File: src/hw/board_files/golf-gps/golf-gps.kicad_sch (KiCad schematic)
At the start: 0 parts

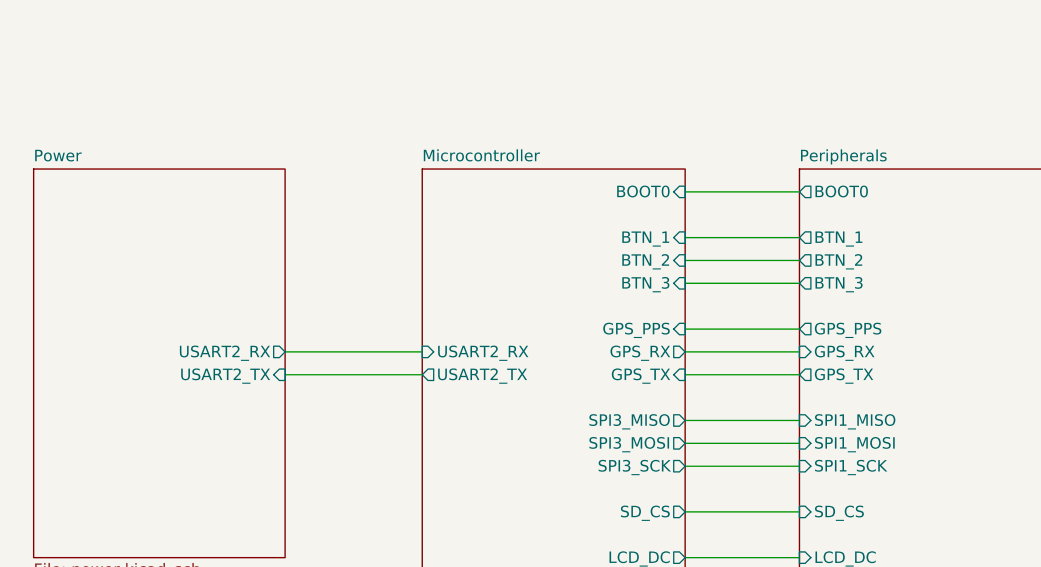
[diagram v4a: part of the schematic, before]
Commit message: Removed USB to UART bridge, added VDDA decoupling, adjusted MCU pinout and updated spreadsheet
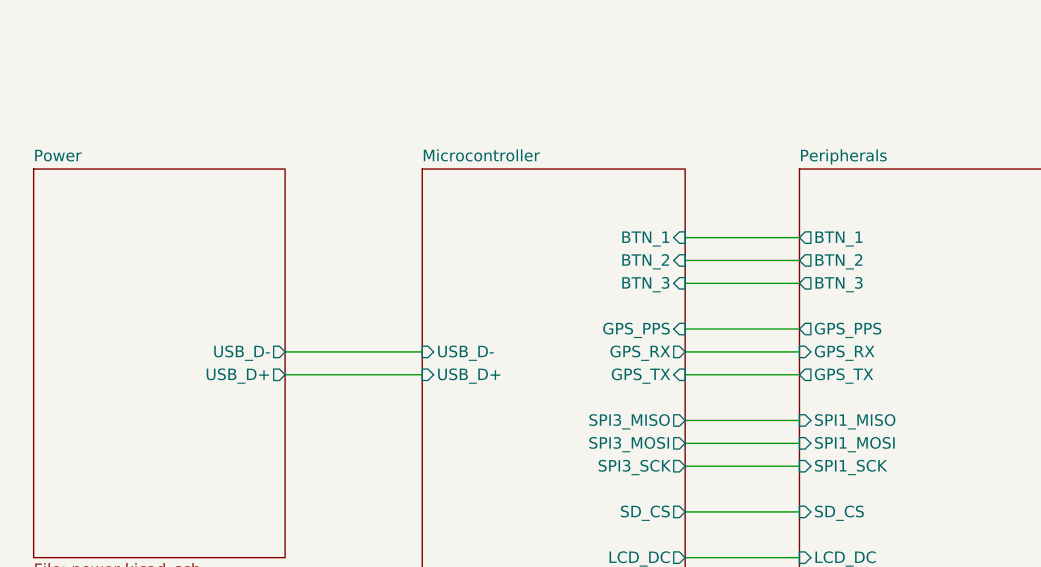
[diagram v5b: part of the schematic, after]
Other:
- sheet Microcontroller ports: added USB_D+, USB_D-; removed BOOT0, USART2_RX, USART2_TX
- sheet Peripherals ports: added none; removed BOOT0
- sheet Power ports: added USB_D+, USB_D-; removed USART2_RX, USART2_TX
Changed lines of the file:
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@@
+	(wire
+		(pts
+			(xy 74.93 80.01) (xy 90.17 80.01)
+		)
+		(stroke
+			(width 0)
+			(type default)
+		)
+	)
 	(wire
 		(pts
@@
 	(wire
 		(pts
-			(xy 74.93 80.01) (xy 90.17 80.01)
-		)
-		(stroke
-			(width 0)
-			(type default)
-		)
-	)
-	(wire
-		(pts
-			(xy 119.38 59.69) (xy 132.08 59.69)
-		)
-		(stroke
-			(width 0)
-			(type default)
-		)
-	)
-	(wire
-		(pts
 			(xy 119.38 85.09) (xy 132.08 85.09)
 		)
@@
 	(wire
 		(pts
+			(xy 74.93 77.47) (xy 90.17 77.47)
+		)
+		(stroke
+			(width 0)
+			(type default)
+		)
+	)
+	(wire
+		(pts
 			(xy 119.38 64.77) (xy 132.08 64.77)
 		)
@@
 		(pts
 			(xy 119.38 95.25) (xy 132.08 95.25)
-		)
-		(stroke
-			(width 0)
-			(type default)
-		)
-	)
-	(wire
-		(pts
-			(xy 74.93 77.47) (xy 90.17 77.47)
 		)
 		(stroke
@@
 			)
 		)
-		(pin "BOOT0" input
-			(at 119.38 59.69 0)
-			(effects
-				(font
-					(size 1.27 1.27)
-				)
-				(justify right)
-			)
-		)
 		(pin "LCD_CS" output
 			(at 119.38 102.87 0)
@@
 			)
 		)
-		(pin "USART2_TX" output
-			(at 90.17 80.01 180)
-			(effects
-				(font
-					(size 1.27 1.27)
-				)
-				(justify left)
-			)
-		)
-		(pin "USART2_RX" input
-			(at 90.17 77.47 180)
-			(effects
-				(font
-					(size 1.27 1.27)
-				)
-				(justify left)
-			)
-		)
 		(pin "GPS_RX" output
 			(at 119.38 77.47 0)
@@
 				)
 				(justify right)
+			)
+		)
+		(pin "USB_D+" input
+			(at 90.17 80.01 180)
+			(effects
+				(font
+					(size 1.27 1.27)
+				)
+				(justify left)
+			)
+		)
+		(pin "USB_D-" input
+			(at 90.17 77.47 180)
+			(effects
+				(font
+					(size 1.27 1.27)
+				)
+				(justify left)
 			)
 		)
@@
 			)
 		)
-		(pin "BOOT0" output
-			(at 132.08 59.69 180)
-			(effects
-				(font
-					(size 1.27 1.27)
-				)
-				(justify left)
-			)
-		)
 		(pin "GPS_RX" input
 			(at 132.08 77.47 180)
@@
 			)
 		)
-		(pin "USART2_TX" input
+		(pin "USB_D-" output
+			(at 74.93 77.47 0)
+			(effects
+				(font
+					(size 1.27 1.27)
+				)
+				(justify right)
+			)
+		)
+		(pin "USB_D+" output
 			(at 74.93 80.01 0)
 			(effects
 				(font
-					(size 1.27 1.27)
-				)
-				(justify right)
-			)
-		)
-		(pin "USART2_RX" output
-			(at 74.93 77.47 0)
-			(effects
-				(font

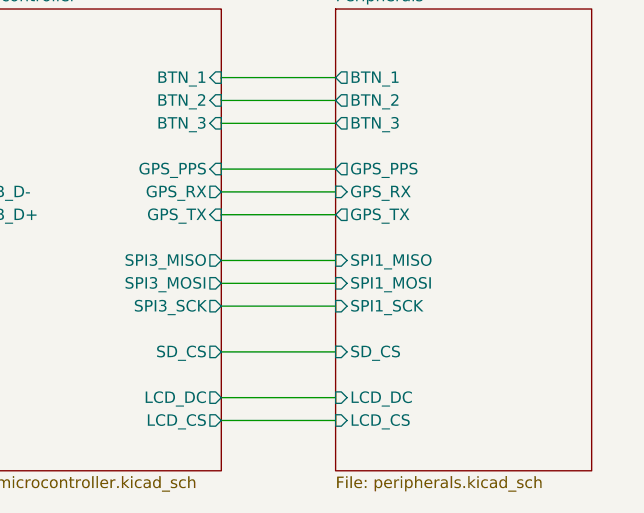
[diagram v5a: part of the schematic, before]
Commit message: Updated pinout and spreadsheet, PCB changes
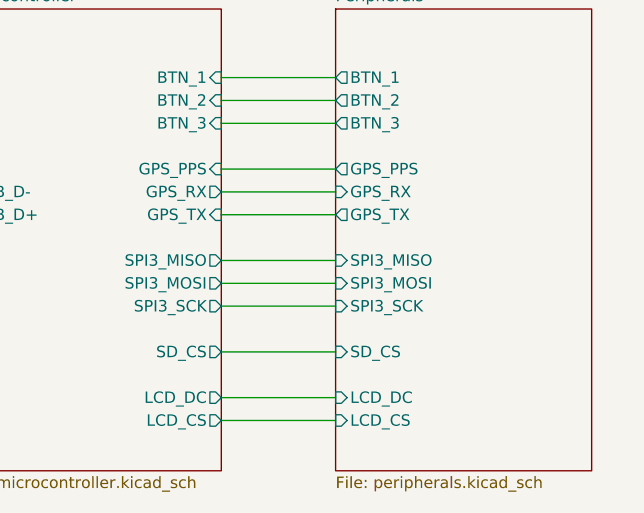
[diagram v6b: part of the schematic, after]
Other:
- sheet Peripherals ports: added SPI3_MISO, SPI3_MOSI, SPI3_SCK; removed SPI1_MISO, SPI1_MOSI, SPI1_SCK
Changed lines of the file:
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@@
 			)
 		)
-		(pin "SPI3_MOSI" output
-			(at 119.38 87.63 0)
+		(pin "USB_D+" input
+			(at 90.17 80.01 180)
 			(effects
 				(font
 					(size 1.27 1.27)
 				)
-				(justify right)
+				(justify left)
+			)
+		)
+		(pin "USB_D-" input
+			(at 90.17 77.47 180)
+			(effects
+				(font
+					(size 1.27 1.27)
+				)
+				(justify left)
 			)
 		)
@@
 			)
 		)
-		(pin "USB_D+" input
-			(at 90.17 80.01 180)
+		(pin "SPI3_MOSI" output
+			(at 119.38 87.63 0)
 			(effects
 				(font
 					(size 1.27 1.27)
 				)
-				(justify left)
-			)
-		)
-		(pin "USB_D-" input
-			(at 90.17 77.47 180)
-			(effects
-				(font
-					(size 1.27 1.27)
-				)
-				(justify left)
+				(justify right)
 			)
 		)
@@
 			)
 		)
-		(pin "SPI1_MOSI" input
+		(pin "SPI3_SCK" input
+			(at 132.08 90.17 180)
+			(effects
+				(font
+					(size 1.27 1.27)
+				)
+				(justify left)
+			)
+		)
+		(pin "SPI3_MOSI" input
 			(at 132.08 87.63 180)
 			(effects
@@
 			)
 		)
-		(pin "SPI1_SCK" input
-			(at 132.08 90.17 180)
-			(effects
-				(font
-					(size 1.27 1.27)
-				)
-				(justify left)
-			)
-		)
-		(pin "SPI1_MISO" input
+		(pin "SPI3_MISO" input
 			(at 132.08 85.09 180)
 			(effects
